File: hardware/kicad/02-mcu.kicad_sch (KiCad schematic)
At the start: 6 parts, among them U1 ESP32-S3-N16R8

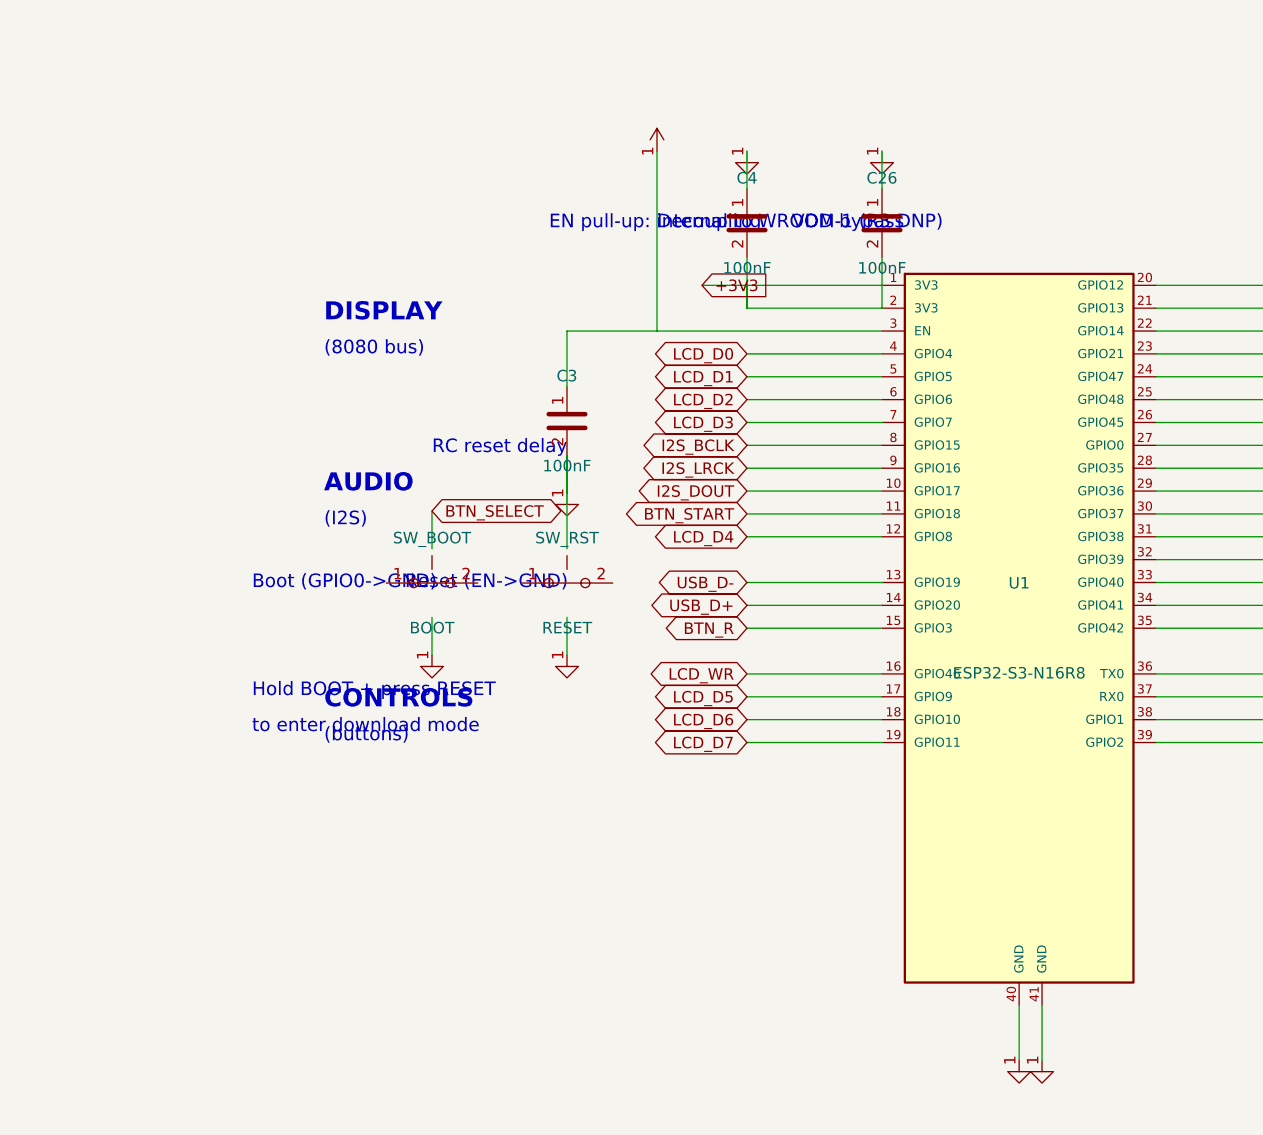
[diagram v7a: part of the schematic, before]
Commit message: sch(layout): fix annotation overlaps across all 6 sheets — reflow to A3 where needed
Root cause: multiple sheets had annotation text boxes placed too close
to each other or to component symbols/net labels. On the live website
this rendered as strings running through each other and through
component pins — unreadable in the schematic viewer.

Per-sheet fixes:

* Sheet 1 — Power Supply
  - Upgraded to A3 landscape (was A4). USB ESD (U4/R22/R23) had
    been placed at (45, 160) directly on top of SW_PWR, C1, U3
    and C2 — all at y=160. There was no room on A4 to fit both
    the input stage (USB-C + IP5306 + battery) and the output
    stage (AMS1117 + LEDs + power switch + USB ESD) with clean
    annotations.
  - USB ESD block relocated to its own dedicated row (y=140).
  - CHARGING INDICATOR LEDs moved to a dedicated right-side zone
    (x=275, y=145) so they no longer collide with USB ESD.
  - POWER SWITCH moved to its own right-side zone (x=285, y=200)
    so its long "v1 as-built" help text no longer crosses through
    C1 / U3 (AMS1117) / C2.
  - VOLTAGE REGULATOR title + AMS1117 area pushed down (y=175 /
    y=200) with DESIGN NOTES following (y=240).
  - C18 (BAT bypass) moved left of Q1, out of the "P-MOSFET RPP /
    SI2301CDS" label zone; C27 (HF bypass) spaced further from C19
    (was 15mm gap, now 22mm) so "VOUT bulk" label no longer runs
    into "HF bypass".
  - Q1 dual annotation stacked with 3mm vertical spacing (was 2mm).
  - R24 label moved BELOW its symbol as "Q1 gate PD".
  - J3 / BT1 pushed further right (jst_x=268, bt_x=315) to use A3
    width and clear the Q1 cluster.

* Sheet 2 — MCU (ESP32-S3)
  - EN pull-up annotation shortened + moved up so it no longer
    collides with the "RC reset delay" label below.
  - BOOT switch pushed further down (c_en_y + 55) and left of the
    RESET switch so its BTN_SELECT glabel and help text no longer
    overlap the DISPLAY / AUDIO / CONTROLS annotation column. Help
    text now sits below the switch in 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
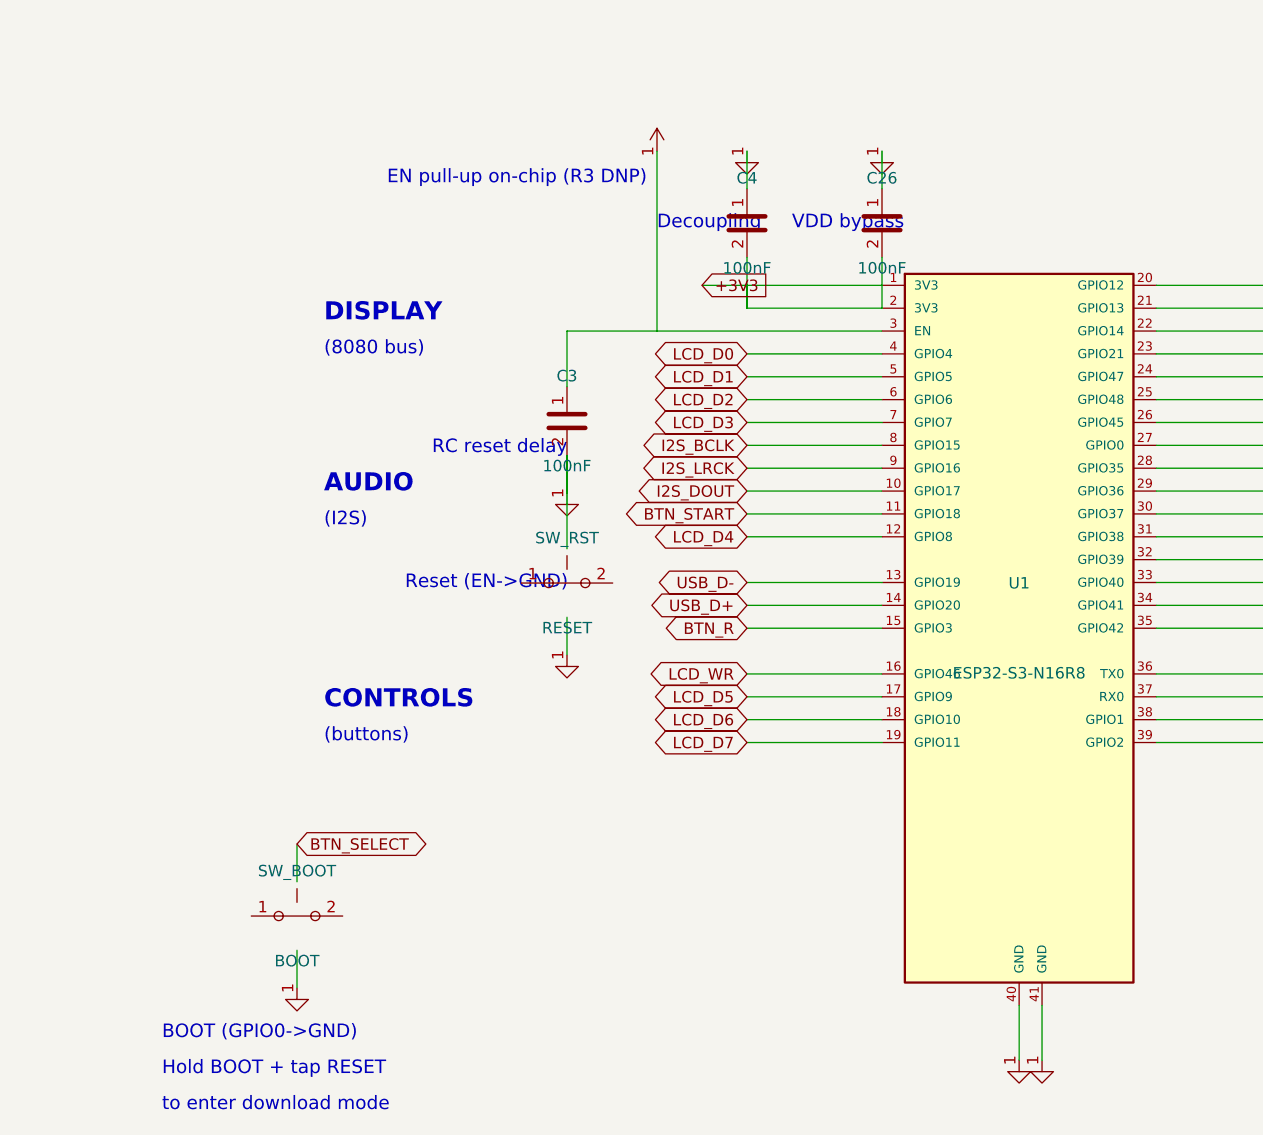
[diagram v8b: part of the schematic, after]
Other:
- note added: "BOOT (GPIO0->GND)"
- note added: "EN pull-up on-chip (R3 DNP)"
- note added: "Hold BOOT + tap RESET"
- note removed: "Boot (GPIO0->GND)"
- note removed: "EN pull-up: internal to WROOM-1 (R3 DNP)"
- note removed: "Hold BOOT + press RESET"
- moved on the sheet: SW_BOOT
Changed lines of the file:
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@@
   (wire (pts (xy 159.76 117) (xy 159.76 136.98)) (stroke (width 0) (type default)))
   (wire (pts (xy 184.76 136.98) (xy 159.76 136.98)) (stroke (width 0) (type default)))
-  (text "EN pull-up: internal to WROOM-1 (R3 DNP)" (at 147.76 125 0) (effects (font (size 1.5 1.5)) (justify left)))
+  (text "EN pull-up on-chip (R3 DNP)" (at 129.76 120 0) (effects (font (size 1.5 1.5)) (justify left)))
   (symbol (lib_id "C") (at 149.76 146.98 0) (unit 1) (exclude_from_sim no) (in_bom yes) (on_board yes) (dnp no) (property "Reference" "C3" (at 149.76 141.98 0) (effects (font (size 1.27 1.27)))) (property "Value" "100nF" (at 149.76 151.98 0) (effects (font (size 1.27 1.27)))) (pin "1") (pin "2"))
   (wire (pts (xy 159.76 136.98) (xy 149.76 136.98)) (stroke (width 0) (type default)))
@@
   (wire (pts (xy 149.76 168.79) (xy 149.76 172.98)) (stroke (width 0) (type default)))
   (text "Reset (EN->GND)" (at 131.76 164.98 0) (effects (font (size 1.5 1.5)) (justify left)))
-  (symbol (lib_id "SW_Push") (at 134.76 164.98 0) (unit 1) (exclude_from_sim no) (in_bom yes) (on_board yes) (dnp no) (property "Reference" "SW_BOOT" (at 134.76 159.98 0) (effects (font (size 1.27 1.27)))) (property "Value" "BOOT" (at 134.76 169.98 0) (effects (font (size 1.27 1.27)))) (pin "1") (pin "2"))
-  (global_label "BTN_SELECT" (shape bidirectional) (at 134.76 156.98 0) (effects (font (size 1.27 1.27))) (property "Intersheetrefs" "" (at 0 0 0) (effects (font (size 1.27 1.27)) hide)))
-  (wire (pts (xy 134.76 161.17) (xy 134.76 156.98)) (stroke (width 0) (type default)))
-  (symbol (lib_id "GND") (at 134.76 172.98 0) (unit 1) (exclude_from_sim no) (in_bom no) (on_board no) (dnp no) (property "Reference" "#PWR004" (at 134.76 170.98 0) (effects (font (size 1.27 1.27)) hide)) (property "Value" "GND" (at 134.76 174.98 0) (effects (font (size 1.27 1.27)) hide)) (pin "1"))
-  (wire (pts (xy 134.76 168.79) (xy 134.76 172.98)) (stroke (width 0) (type default)))
-  (text "Boot (GPIO0->GND)" (at 114.75999999999999 164.98 0) (effects (font (size 1.5 1.5)) (justify left)))
-  (text "Hold BOOT + press RESET" (at 114.75999999999999 176.98 0) (effects (font (size 1.5 1.5)) (justify left)))
-  (text "to enter download mode" (at 114.75999999999999 180.98 0) (effects (font (size 1.5 1.5)) (justify left)))
+  (symbol (lib_id "SW_Push") (at 119.75999999999999 201.98 0) (unit 1) (exclude_from_sim no) (in_bom yes) (on_board yes) (dnp no) (property "Reference" "SW_BOOT" (at 119.75999999999999 196.98 0) (effects (font (size 1.27 1.27)))) (property "Value" "BOOT" (at 119.75999999999999 206.98 0) (effects (font (size 1.27 1.27)))) (pin "1") (pin "2"))
+  (global_label "BTN_SELECT" (shape bidirectional) (at 119.75999999999999 193.98 0) (effects (font (size 1.27 1.27))) (property "Intersheetrefs" "" (at 0 0 0) (effects (font (size 1.27 1.27)) hide)))
+  (wire (pts (xy 119.75999999999999 198.17) (xy 119.75999999999999 193.98)) (stroke (width 0) (type default)))
+  (symbol (lib_id "GND") (at 119.75999999999999 209.98 0) (unit 1) (exclude_from_sim no) (in_bom no) (on_board no) (dnp no) (property "Reference" "#PWR004" (at 119.75999999999999 207.98 0) (effects (font (size 1.27 1.27)) hide)) (property "Value" "GND" (at 119.75999999999999 211.98 0) (effects (font (size 1.27 1.27)) hide)) (pin "1"))
+  (wire (pts (xy 119.75999999999999 205.79) (xy 119.75999999999999 209.98)) (stroke (width 0) (type default)))
+  (text "BOOT (GPIO0->GND)" (at 104.75999999999999 214.98 0) (effects (font (size 1.5 1.5)) (justify left)))
+  (text "Hold BOOT + tap RESET" (at 104.75999999999999 218.98 0) (effects (font (size 1.5 1.5)) (justify left)))
+  (text "to enter download mode" (at 104.75999999999999 222.98 0) (effects (font (size 1.5 1.5)) (justify left)))
   (symbol (lib_id "C") (at 169.76 125 0) (unit 1) (exclude_from_sim no) (in_bom yes) (on_board yes) (dnp no) (property "Reference" "C4" (at 169.76 120 0) (effects (font (size 1.27 1.27)))) (property "Value" "100nF" (at 169.76 130 0) (effects (font (size 1.27 1.27)))) (pin "1") (pin "2"))
   (wire (pts (xy 169.76 128.81) (xy 169.76 134.44)) (stroke (width 0) (type default)))
